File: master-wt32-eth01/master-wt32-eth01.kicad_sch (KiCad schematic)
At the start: 23 parts, among them J1 24V Field, J2 24V System, J3 Enable, J4 Screw_Terminal_01x03, J5 Conn_01x06_Female, J6 Conn_01x06_Female, SW1 SW_DIP_x03, U1 LM2596-Board, U2 WT32-ETH0-Board, U3 PC817

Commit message: refactor power
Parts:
- removed C1, C2: 1uF 50V, Capacitor_THT:CP_Radial_D5.0mm_P2.50mm, symbol Device:C_Polarized
- removed C3, C4: 100nF 63V, Capacitor_THT:C_Rect_L7.0mm_W2.0mm_P5.00mm, symbol Device:C
- removed D1, D2: DB107, custom:DB107, symbol custom:DB107
- removed J1: 24V Field, TerminalBlock:TerminalBlock_bornier-2_P5.08mm, symbol Connector:Screw_Terminal_01x02
- removed J2: 24V System, TerminalBlock:TerminalBlock_bornier-2_P5.08mm, symbol Connector:Screw_Terminal_01x02
- removed J3: Enable, TerminalBlock:TerminalBlock_bornier-2_P5.08mm, symbol Connector:Screw_Terminal_01x02
- removed U1: LM2596-Board, boards:LM2596-Board, symbol boards:LM2596-Board
- added J1: Screw_Terminal_01x06, TerminalBlock:TerminalBlock_bornier-6_P5.08mm, symbol Connector:Screw_Terminal_01x06
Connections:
- net +24V: now also SW1.3, J1.6 (Pin_6); no longer SW1.4, SW1.6
- net GNDPWR: no longer SW1.5
- net SYSTEM+: now also SW1.5, SW1.6, J1.3 (Pin_3); no longer SW1.1
- net SYSTEM-: now also J1.4 (Pin_4); no longer SW1.2
- net ENABLE_IN: now reaches R2.2
- net ENABLE_IN: now also SW1.4, J1.5 (Pin_5); no longer SW1.3
- new net FIELD+: J1.1 (Pin_1), SW1.1
- new net FIELD-: J1.2 (Pin_2), SW1.2
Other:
- added sheet power-24v (../include/power-24v.kicad_sch)
- added sheet power-3.3v-lm2596-board (../include/power-3.3v-lm2596-board.kicad_sch)
- moved on the sheet: H1, H2, H3, H4, J4, J5, J6, R1, R2, R3, U2, U3

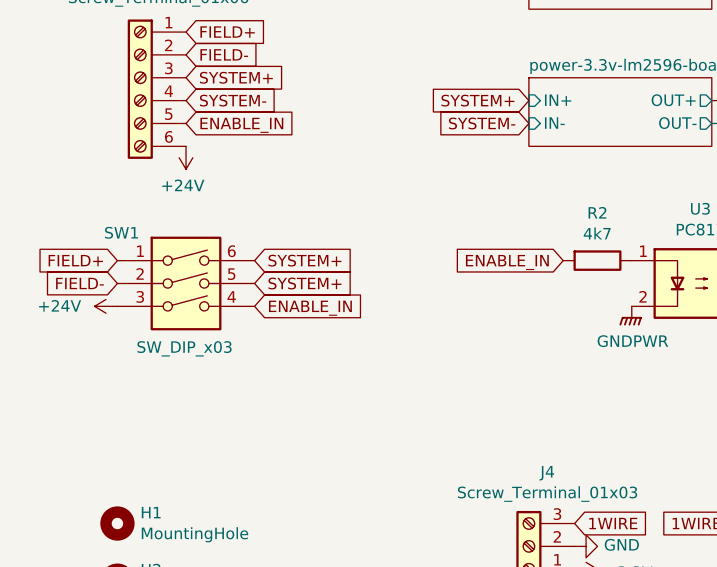
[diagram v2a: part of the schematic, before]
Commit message: fix power wiring in master-wt32-eth01
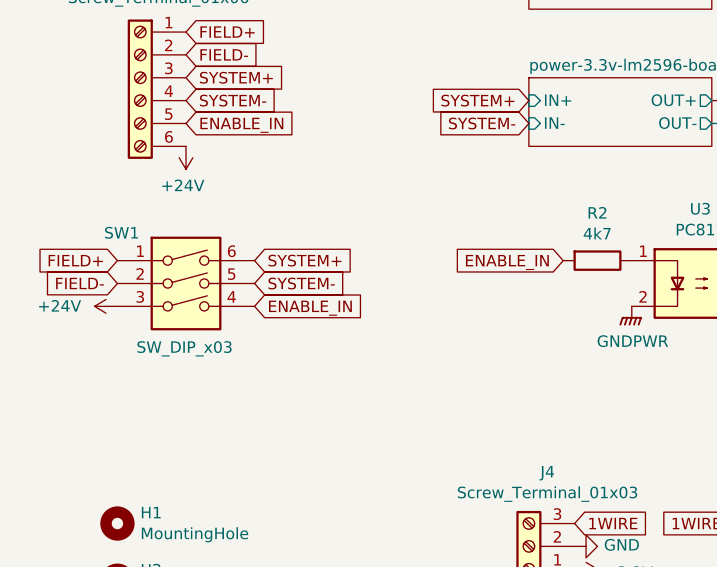
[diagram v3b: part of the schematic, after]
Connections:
- net SYSTEM+: no longer SW1.5
- net SYSTEM-: now also SW1.5
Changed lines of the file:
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@@
     )
   )
-  (global_label "SYSTEM+" (shape input) (at 46.99 60.96 0) (fields_autoplaced)
+  (global_label "SYSTEM-" (shape input) (at 46.99 60.96 0) (fields_autoplaced)
     (effects (font (size 1.27 1.27)) (justify left))
-    (property "Intersheet References" "${INTERSHEET_REFS}" (id 0) (at 58.0512 60.8806 0)
+    (property "Intersheet References" "${INTERSHEET_REFS}" (id 0) (at 58.0512 61.0394 0)
       (effects (font (size 1.27 1.27)) (justify left) hide)
     )
